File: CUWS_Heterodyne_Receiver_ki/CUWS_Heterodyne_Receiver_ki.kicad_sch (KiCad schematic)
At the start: 0 parts

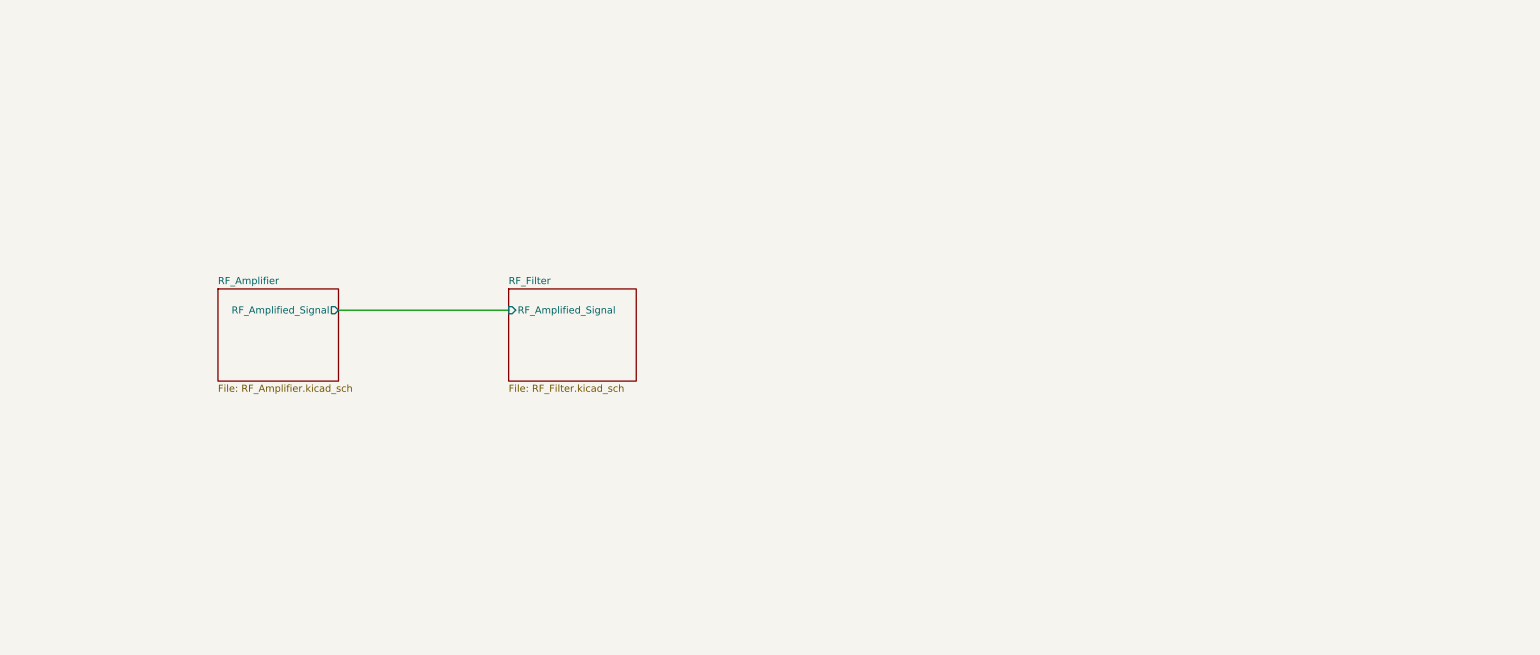
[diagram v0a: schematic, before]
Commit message: Finalised first draft of top hierarchy
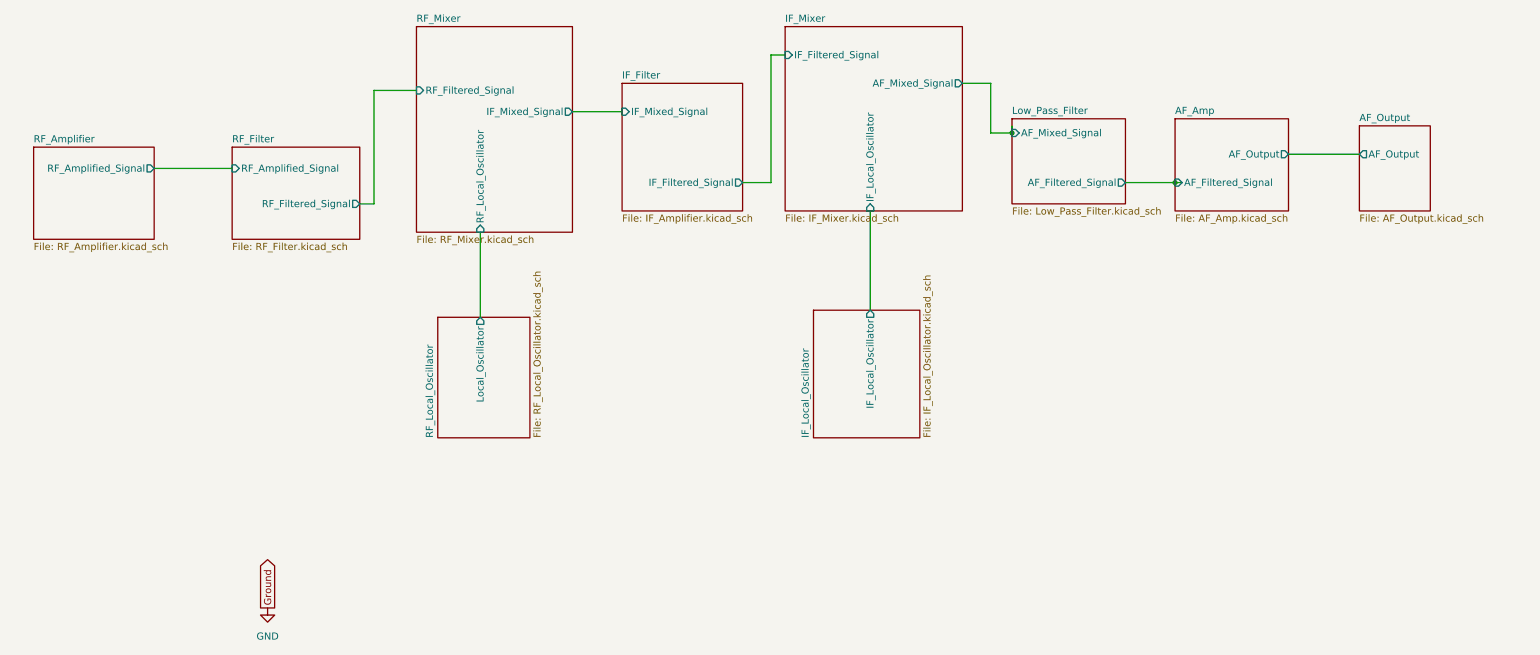
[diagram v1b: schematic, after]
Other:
- added sheet AF_Amp (AF_Amp.kicad_sch)
- added sheet AF_Output (AF_Output.kicad_sch)
- added sheet IF_Filter (IF_Amplifier.kicad_sch)
- added sheet IF_Local_Oscillator (IF_Local_Oscillator.kicad_sch)
- added sheet IF_Mixer (IF_Mixer.kicad_sch)
- added sheet Low_Pass_Filter (Low_Pass_Filter.kicad_sch)
- added sheet RF_Local_Oscillator (RF_Local_Oscillator.kicad_sch)
- added sheet RF_Mixer (RF_Mixer.kicad_sch)
- sheet RF_Filter ports: added RF_Filtered_Signal; removed none
